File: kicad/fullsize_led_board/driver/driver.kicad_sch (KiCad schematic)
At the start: 131 parts, among them J4 Anodes Header, J5 Cathodes Header, Q1 SQ2351CES, Q10 SQ2351CES, Q11 SQ2351CES, Q12 SQ2351CES, Q13 SQ2351CES, Q14 SQ2351CES, Q15 SQ2351CES, Q16 SQ2351CES, Q17 SQ2351CES, Q18 SQ2351CES, Q19 SQ2351CES, Q2 SQ2351CES, Q20 SQ2351CES, Q21 SQ2351CES, Q22 SQ2351CES, Q23 SQ2351CES, Q24 SQ2351CES, Q3 SQ2351CES, Q4 SQ2351CES, Q5 SQ2351CES, Q6 SQ2351CES, Q7 SQ2351CES, Q8 SQ2351CES, Q9 SQ2351CES, U1 74HCT541, U2 74HCT595, U3 74HCT595, U4 74HCT595, U5 TPIC6B595N, U6 TPIC6B595N, U7 TPIC6B595N, U8 TPIC6B595N

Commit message: fullsize led board: set pull up resistor values in schematic
The 1M ohms was too low as I could pull the high-side switches' gates down with my body when touching those lines.
100K was better as the transistor delivered less current but 10K managed to completely shut it off.
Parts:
- R1, R11, R13, R15, R17, R19, R2, R21, R23, R25, R27, R29, R3, R31, R33, R35, R37, R39, R4, R41, R43, R45, R47, R49, R5, R51, R53, R6, R7, R9: value R -> 10K
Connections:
- net +5V: now also R1.2, R3.2, R4.2, R5.2, R6.2; no longer R1.1, R3.1, R4.1, R5.1, R6.1
- net ApplyRowAndStrobe: now also J3.1 (Pin_1), J3.2 (Pin_2), J3.3 (Pin_3), J3.6 (Pin_6), R1.1, R3.1, R4.1, R5.1, R6.1, U1.2 (A0), U1.3 (A1), U1.5 (A3), U1.7 (A5); no longer R4.2
- removed net RowData: J3.1 (Pin_1), R6.2, U1.2 (A0)
- removed net RowStrobe: J3.2 (Pin_2), R3.2, U1.5 (A3)
- removed net ShiftRowData: J3.3 (Pin_3), R5.2, U1.3 (A1)
- removed net ~{OutputEnable}: J3.6 (Pin_6), R1.2, U1.7 (A5)

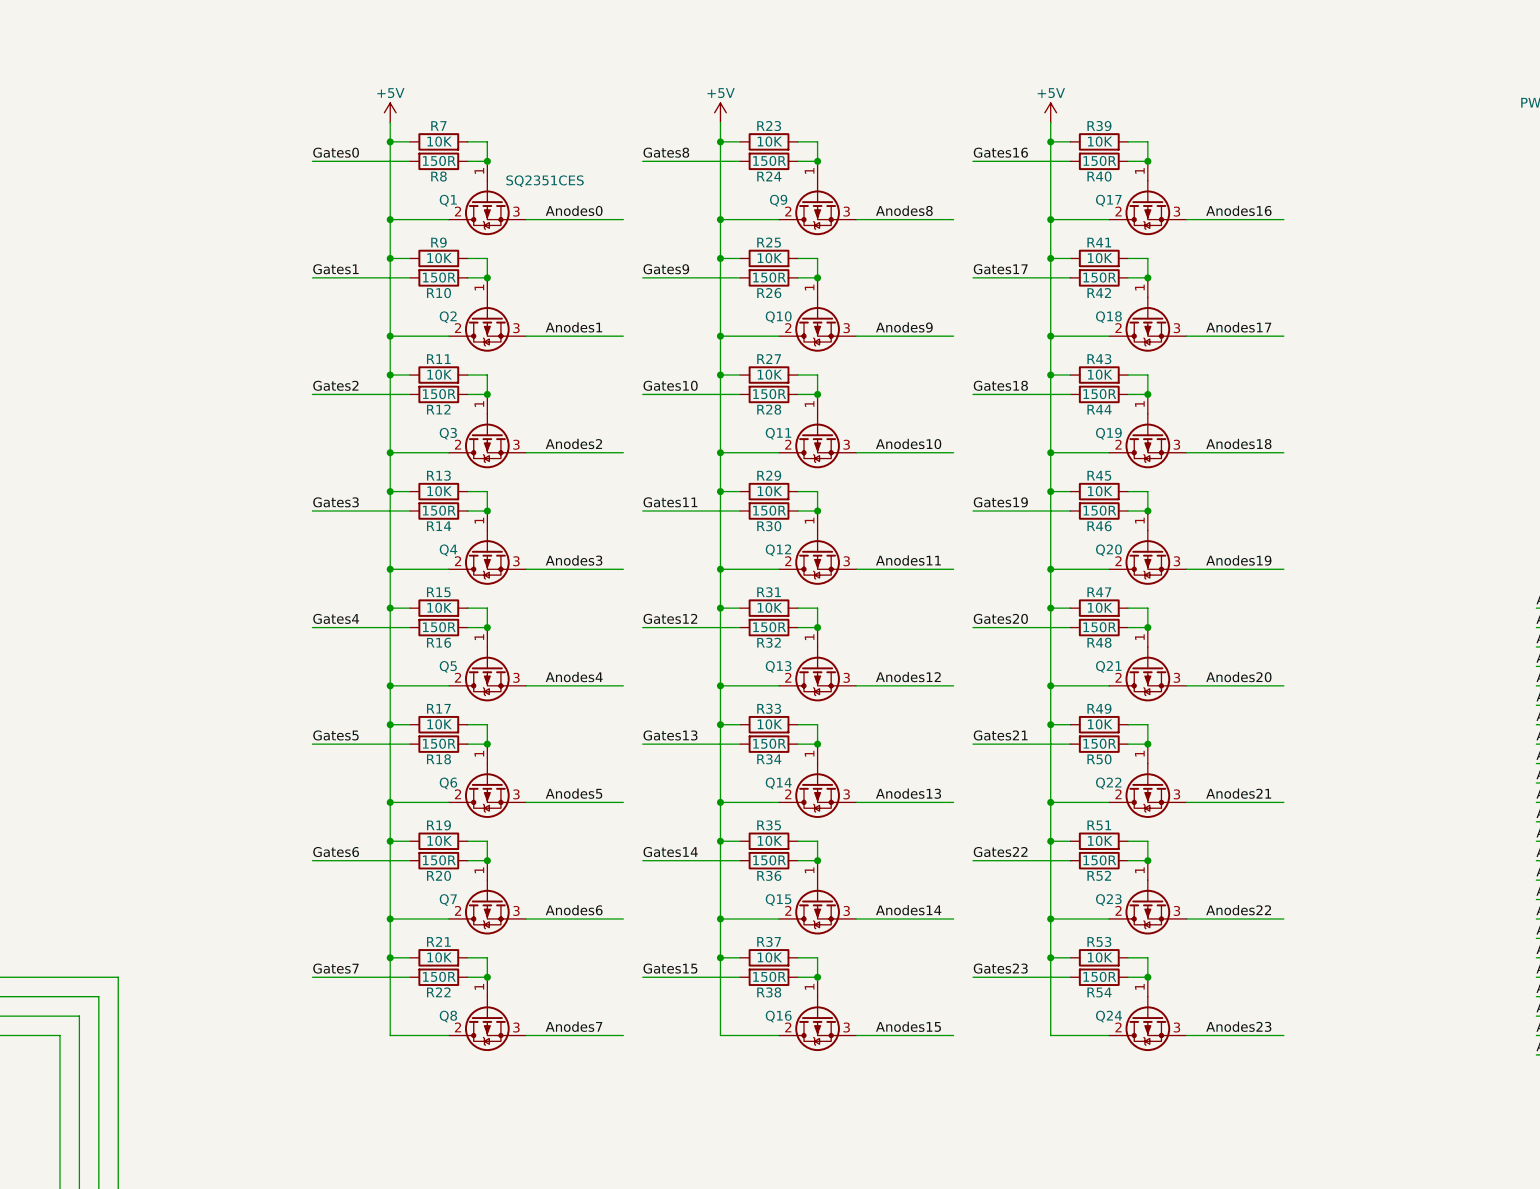
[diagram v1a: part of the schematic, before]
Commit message: fullsize led board: rearranged high-side resistors to eliminate voltage divier
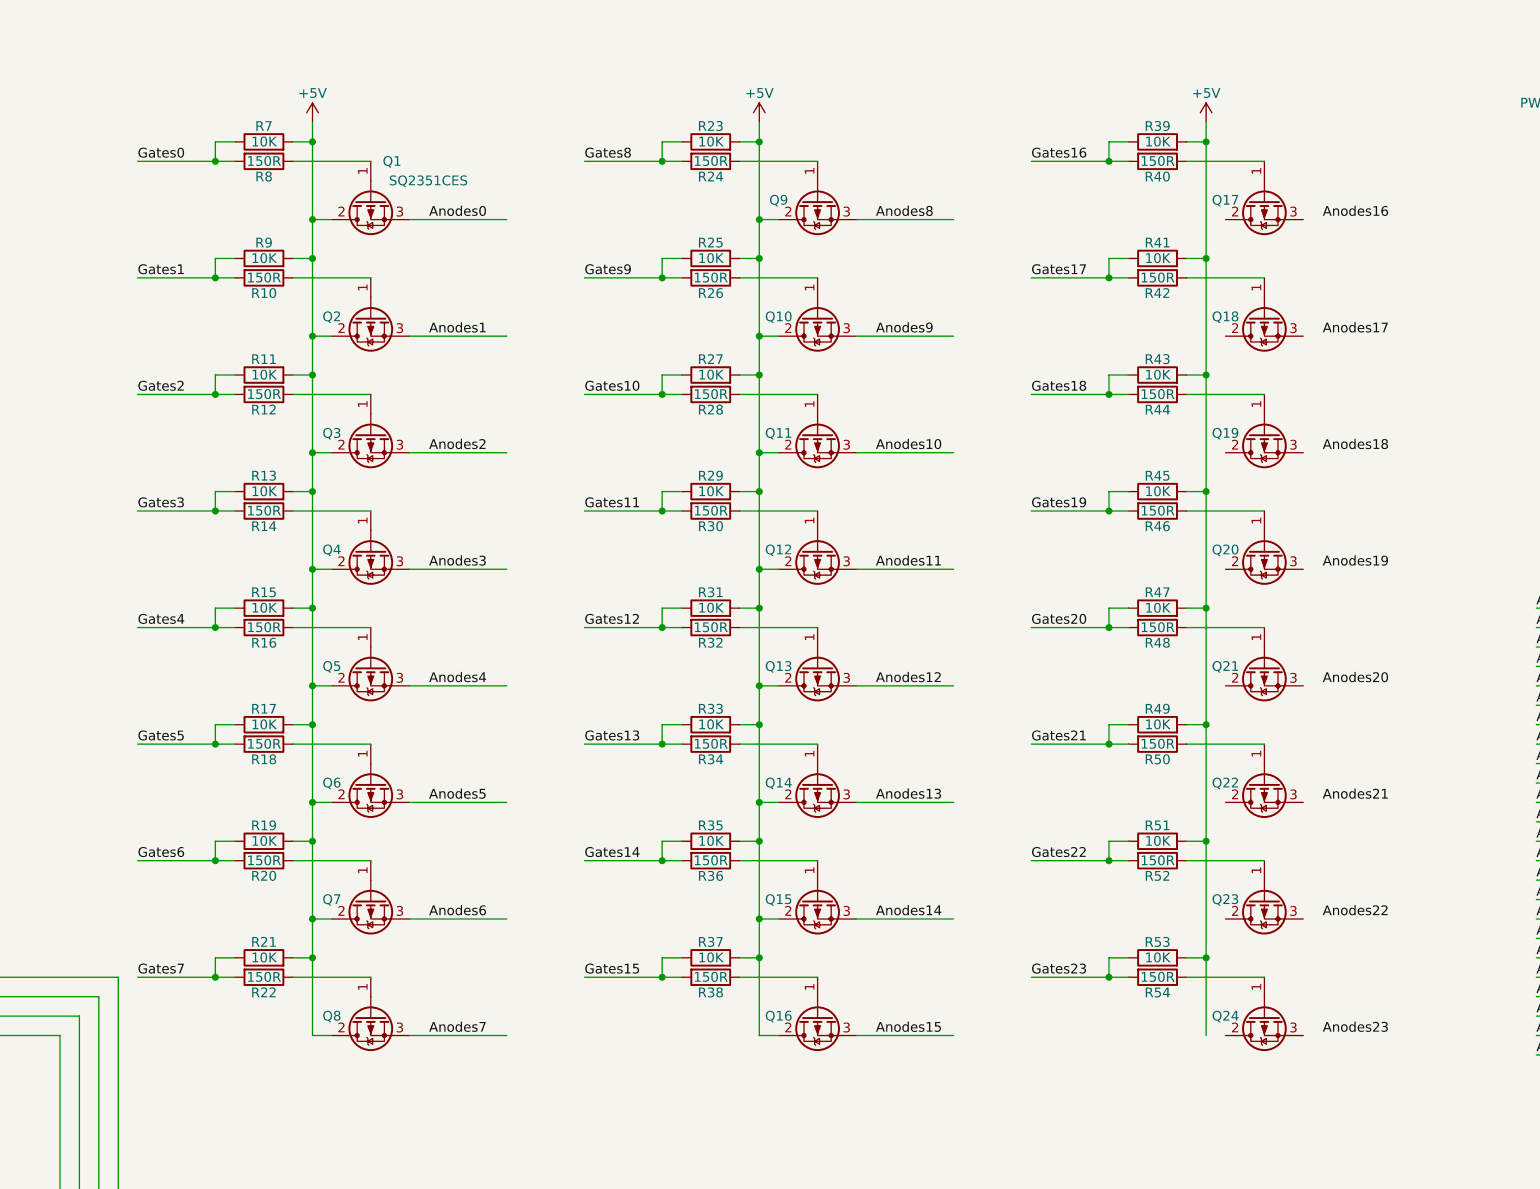
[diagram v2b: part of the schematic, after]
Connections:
- net +5V: now also R11.2, R13.2, R15.2, R17.2, R19.2, R21.2, R23.2, R25.2, R27.2, R29.2, R31.2, R33.2, R35.2, R37.2, R39.2, R41.2, R43.2, R45.2, R47.2, R49.2, R51.2, R53.2, R7.2, R9.2; no longer Q17.2 (S), Q18.2 (S), Q19.2 (S), Q20.2 (S), Q21.2 (S), Q22.2 (S), Q23.2 (S), Q24.2 (S), R11.1, R13.1, R15.1, R17.1, R19.1, R21.1, R23.1, R25.1, R27.1, R29.1, R31.1, R33.1, R35.1, R37.1, R39.1, R41.1, R43.1, R45.1, R47.1, R49.1, R51.1, R53.1, R7.1, R9.1
- net Anodes16: no longer Q17.3 (D)
- net Anodes17: no longer Q18.3 (D)
- net Anodes18: no longer Q19.3 (D)
- net Anodes19: no longer Q20.3 (D)
- net Anodes20: no longer Q21.3 (D)
- net Anodes21: no longer Q22.3 (D)
- net Anodes22: no longer Q23.3 (D)
- net Anodes23: no longer Q24.3 (D)
- net Gates0: now also R7.1
- net Gates1: now also R9.1
- net Gates10: now also R27.1
- net Gates11: now also R29.1
- net Gates12: now also R31.1
- net Gates13: now also R33.1
- net Gates14: now also R35.1
- net Gates15: now also R37.1
- net Gates16: now also R39.1
- net Gates17: now also R41.1
- net Gates18: now also R43.1
- net Gates19: now also R45.1
- net Gates2: now also R11.1
- net Gates20: now also R47.1
- net Gates21: now also R49.1
- net Gates22: now also R51.1
- net Gates23: now also R53.1
- net Gates3: now also R13.1
- net Gates4: now also R15.1
- net Gates5: now also R17.1
- net Gates6: now also R19.1
- net Gates7: now also R21.1
- net Gates8: now also R23.1
- net Gates9: now also R25.1
- net at Q18.1 (G), R42.1: no longer R41.2
- net at Q10.1 (G), R26.1: no longer R25.2
- net at Q12.1 (G), R30.1: no longer R29.2
- net at Q21.1 (G), R48.1: no longer R47.2
- net at Q20.1 (G), R46.1: no longer R45.2
- net at Q22.1 (G), R50.1: no longer R49.2
- net at Q13.1 (G), R32.1: no longer R31.2
- net at Q3.1 (G), R12.1: no longer R11.2
- net at Q14.1 (G), R34.1: no longer R33.2
- net at Q17.1 (G), R40.1: no longer R39.2
- net at Q1.1 (G), R8.1: no longer R7.2
- net at Q11.1 (G), R28.1: no longer R27.2
- net at Q15.1 (G), R36.1: no longer R35.2
- net at Q7.1 (G), R20.1: no longer R19.2
- net at Q16.1 (G), R38.1: no longer R37.2
- net at Q4.1 (G), R14.1: no longer R13.2
- net at Q23.1 (G), R52.1: no longer R51.2
- net at Q8.1 (G), R22.1: no longer R21.2
- net at Q2.1 (G), R10.1: no longer R9.2
- net at Q5.1 (G), R16.1: no longer R15.2
- net at Q24.1 (G), R54.1: no longer R53.2
- net at Q6.1 (G), R18.1: no longer R17.2
- net at Q19.1 (G), R44.1: no longer R43.2
- net at Q9.1 (G), R24.1: no longer R23.2
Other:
- moved on the sheet: Q1, Q17, Q18, Q19, Q2, Q20, Q21, Q22, Q23, Q24, Q3, Q4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

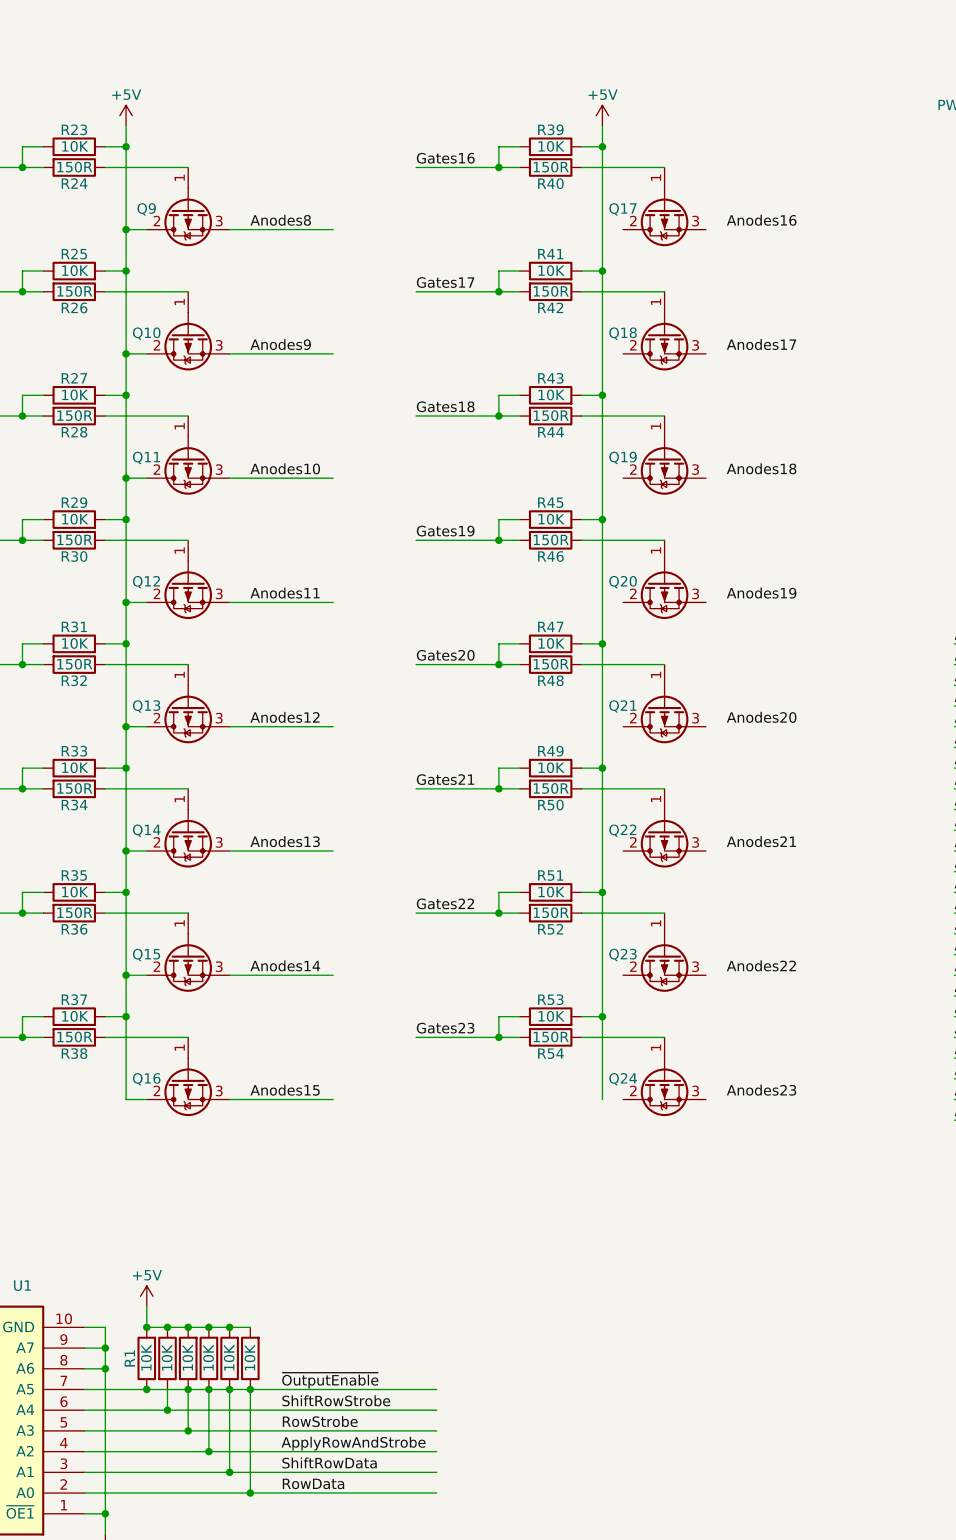
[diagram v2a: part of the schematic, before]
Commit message: fullsize led board: routed pcb completely, silkscreen fix up next
Also some connections were fixed in the schematic.
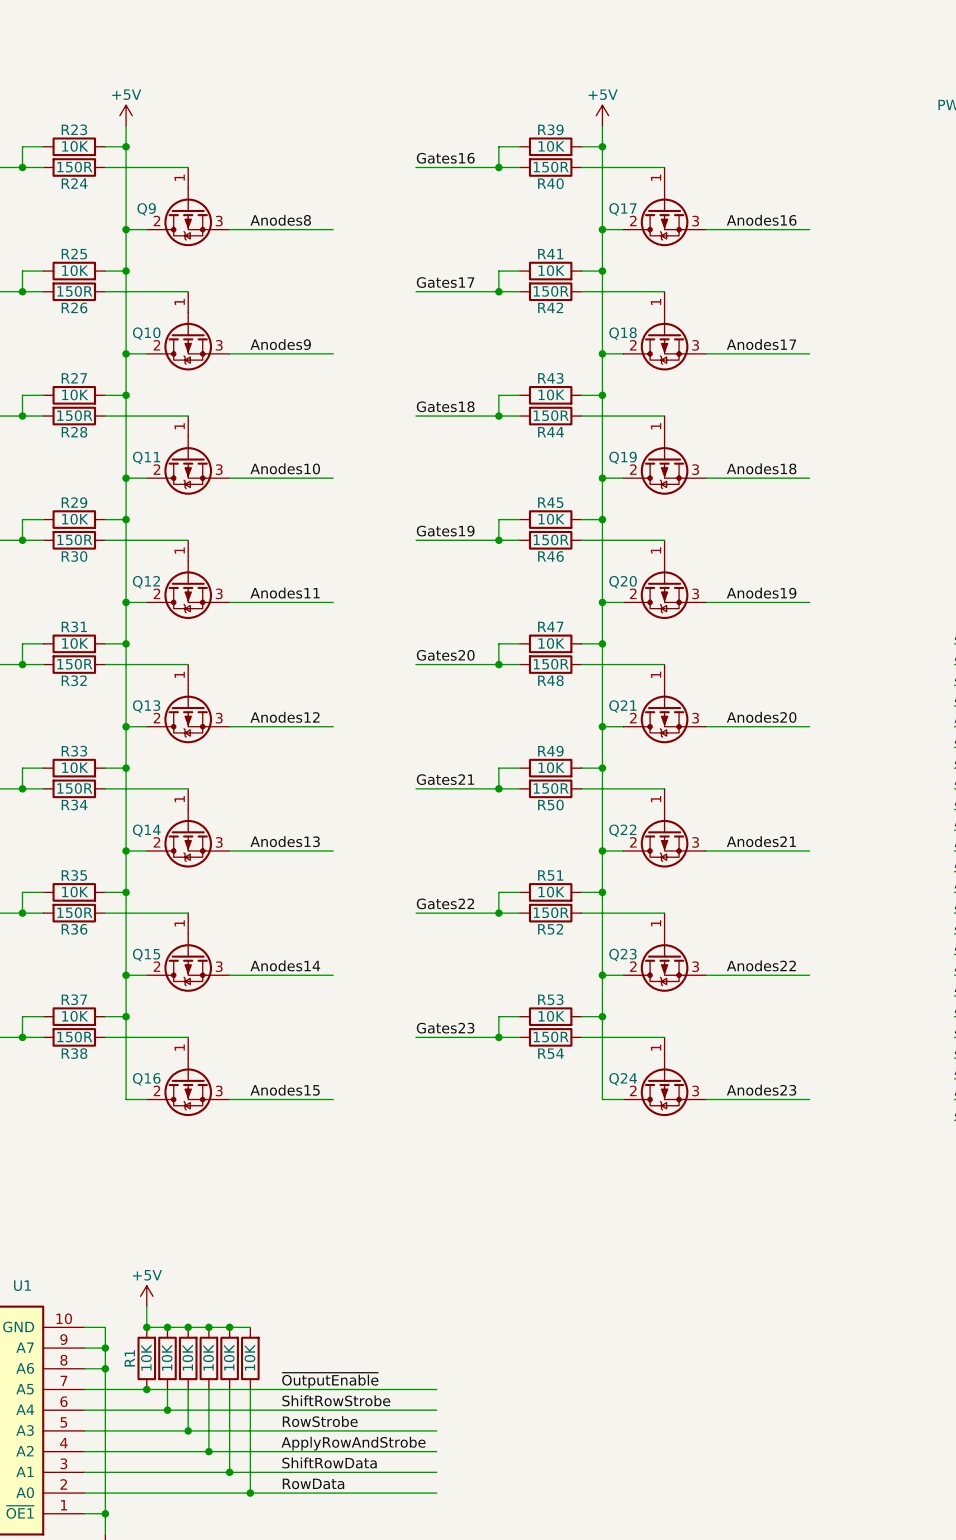
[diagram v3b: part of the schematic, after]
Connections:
- net +5V: now also Q17.2 (S), Q18.2 (S), Q19.2 (S), Q20.2 (S), Q21.2 (S), Q22.2 (S), Q23.2 (S), Q24.2 (S)
- net Anodes16: now also Q17.3 (D)
- net Anodes17: now also Q18.3 (D)
- net Anodes18: now also Q19.3 (D)
- net Anodes19: now also Q20.3 (D)
- net Anodes20: now also Q21.3 (D)
- net Anodes21: now also Q22.3 (D)
- net Anodes22: now also Q23.3 (D)
- net Anodes23: now also Q24.3 (D)
- net ApplyRowAndStrobe: no longer J3.1 (Pin_1), J3.2 (Pin_2), J3.3 (Pin_3), J3.6 (Pin_6), R1.1, R3.1, R5.1, R6.1, U1.2 (A0), U1.3 (A1), U1.5 (A3), U1.7 (A5)
- new net RowData: J3.1 (Pin_1), R6.1, U1.2 (A0)
- new net RowStrobe: J3.2 (Pin_2), R3.1, U1.5 (A3)
- new net ShiftRowData: J3.3 (Pin_3), R5.1, U1.3 (A1)
- new net ~{OutputEnable}: J3.6 (Pin_6), R1.1, U1.7 (A5)
